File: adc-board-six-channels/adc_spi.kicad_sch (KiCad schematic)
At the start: 6 parts, among them U1 ADC_SPI_GEN

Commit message: Generated gerber for adc-board
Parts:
- renumbered C1 to C10, C2 to C11, C3 to C12, R4 to R10, R3 to R9, U1 to U4
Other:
- note added: "[1]"
- note added: "[1] This resistor and capacitor form a low-pass filter at the input of the ADC."
- note added: "[2]"
- note added: "[2] This resistor can be placed to avoid ringing at the data line."
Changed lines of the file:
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@@
     (stroke (width 0) (type default) (color 0 0 0 0))
+  )
+  (text "[1]" (at 72.136 27.305 0)
+    (effects (font (size 1.27 1.27)) (justify left bottom))
+  )
+  (text "[2]" (at 105.029 15.621 0)
+    (effects (font (size 1.27 1.27)) (justify left bottom))
+  )
+  (text "[2] This resistor can be placed to avoid ringing at\nthe data line."
+    (at 126.619 23.241 0)
+    (effects (font (size 1.27 1.27)) (justify left bottom))
+  )
+  (text "[1] This resistor and capacitor form a low-pass filter\nat the input of the ADC."
+    (at 126.873 17.907 0)
+    (effects (font (size 1.27 1.27)) (justify left bottom))
   )
   (label "GND" (at 38.608 26.162 180)
@@
   (symbol (lib_id "Device:R_Small") (at 106.68 20.828 90) (unit 1)
     (in_bom yes) (on_board yes)
-    (property "Reference" "R3" (id 0) (at 106.68 17.272 90))
+    (property "Reference" "R9" (id 0) (at 106.68 17.272 90))
     (property "Value" "47R" (id 1) (at 106.68 19.05 90))
     (property "Footprint" "Resistor_SMD:R_0805_2012Metric_Pad1.20x1.40mm_HandSolder" (id 2) (at 106.68 20.828 0)
@@
   (symbol (lib_id "CL_Analog_ADC:ADC_SPI_GEN") (at 91.694 23.368 0) (unit 1)
     (in_bom yes) (on_board yes)
-    (property "Reference" "U1" (id 0) (at 92.964 16.764 0)
+    (property "Reference" "U4" (id 0) (at 92.964 16.764 0)
       (effects (font (size 1.27 1.27)) (justify left))
     )
@@
   (symbol (lib_id "Device:C_Small") (at 40.386 22.606 0) (unit 1)
     (in_bom yes) (on_board yes)
-    (property "Reference" "C1" (id 0) (at 42.164 21.336 0)
+    (property "Reference" "C10" (id 0) (at 42.164 21.336 0)
       (effects (font (size 1.27 1.27)) (justify left))
     )
@@
   (symbol (lib_id "Device:C_Small") (at 78.486 27.94 0) (unit 1)
     (in_bom yes) (on_board yes)
-    (property "Reference" "C3" (id 0) (at 80.264 26.67 0)
+    (property "Reference" "C12" (id 0) (at 80.264 26.67 0)
       (effects (font (size 1.27 1.27)) (justify left))
     )
@@
   (symbol (lib_id "Device:R_Small") (at 73.66 23.368 90) (unit 1)
     (in_bom yes) (on_board yes)
-    (property "Reference" "R4" (id 0) (at 73.66 19.812 90))
+    (property "Reference" "R10" (id 0) (at 73.66 19.812 90))
     (property "Value" "TBD" (id 1) (at 73.66 21.59 90))
     (property "Footprint" "Resistor_SMD:R_0805_2012Metric_Pad1.20x1.40mm_HandSolder" (id 2) (at 73.66 23.368 0)
@@
   (symbol (lib_id "Device:C_Small") (at 47.752 22.606 0) (unit 1)
     (in_bom yes) (on_board yes)
-    (property "Reference" "C2" (id 0) (at 49.53 21.336 0)
+    (property "Reference" "C11" (id 0) (at 49.53 21.336 0)
       (effects (font (size 1.27 1.27)) (justify left))
     )

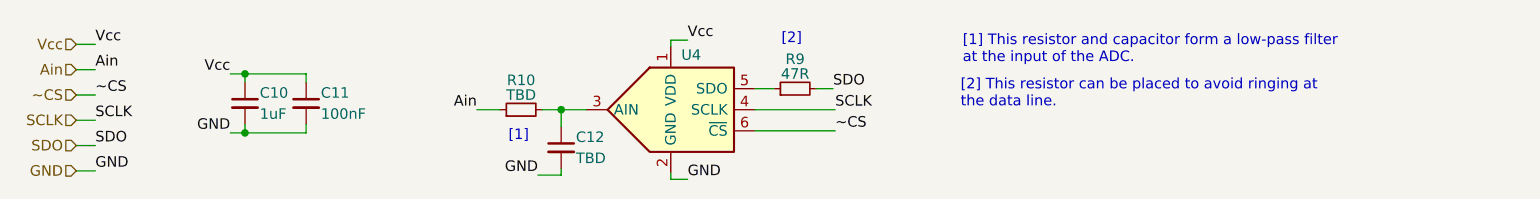
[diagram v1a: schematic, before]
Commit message: Created bom for adc board
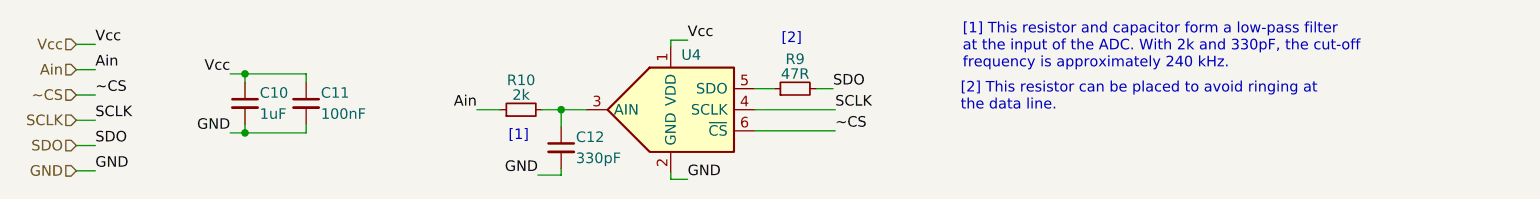
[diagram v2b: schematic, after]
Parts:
- C12: value TBD -> 330pF
- R10: value TBD -> 2k
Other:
- note added: "[1] This resistor and capacitor form a low-pass filter at the input of the ADC. With 2k and 330pF, the cut-off frequency is approximately 240 kHz."
- note removed: "[1] This resistor and capacitor form a low-pass filter at the input of the ADC."
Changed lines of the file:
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@@
   )
   (text "[2] This resistor can be placed to avoid ringing at\nthe data line."
-    (at 126.619 23.241 0)
+    (at 126.619 23.622 0)
     (effects (font (size 1.27 1.27)) (justify left bottom))
   )
-  (text "[1] This resistor and capacitor form a low-pass filter\nat the input of the ADC."
-    (at 126.873 17.907 0)
+  (text "[1] This resistor and capacitor form a low-pass filter\nat the input of the ADC. With 2k and 330pF, the cut-off\nfrequency is approximately 240 kHz."
+    (at 126.873 18.542 0)
     (effects (font (size 1.27 1.27)) (justify left bottom))
   )
@@
       (effects (font (size 1.27 1.27)) (justify left))
     )
-    (property "Value" "TBD" (id 1) (at 80.264 29.21 0)
+    (property "Value" "330pF" (id 1) (at 80.264 29.21 0)
       (effects (font (size 1.27 1.27)) (justify left))
     )
@@
     (in_bom yes) (on_board yes)
     (property "Reference" "R10" (id 0) (at 73.66 19.812 90))
-    (property "Value" "TBD" (id 1) (at 73.66 21.59 90))
+    (property "Value" "2k" (id 1) (at 73.66 21.59 90))
     (property "Footprint" "Resistor_SMD:R_0805_2012Metric_Pad1.20x1.40mm_HandSolder" (id 2) (at 73.66 23.368 0)
       (effects (font (size 1.27 1.27)) hide)
